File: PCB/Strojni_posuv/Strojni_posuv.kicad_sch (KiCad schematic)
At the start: 32 parts, among them SW1 SW_DPST_x2, SW2 SW_DPST_x2, SW3 SW_DPST_x2, SW4 SW_DPST_x2, SW5 SW_DPST_x2, U1 STM32F103RBTx

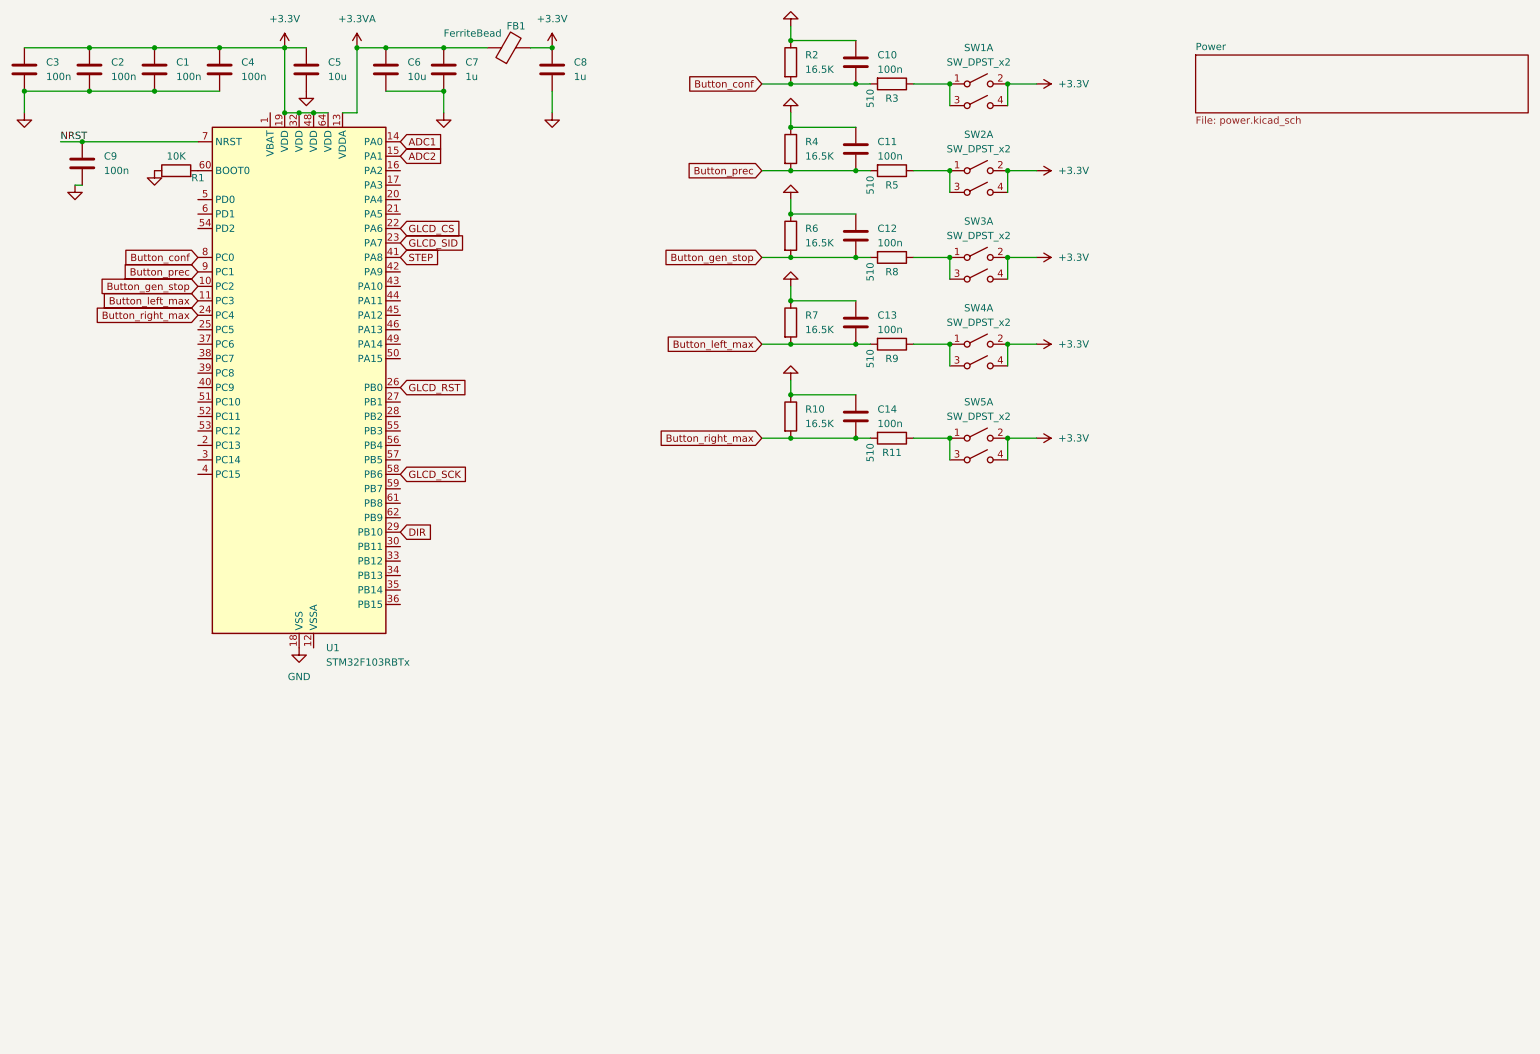
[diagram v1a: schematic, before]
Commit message: Learning, PCB making #2 Added new links to Learning Motor driver part in Kicad, Power part (48V to 5V), New pins to STM32F103
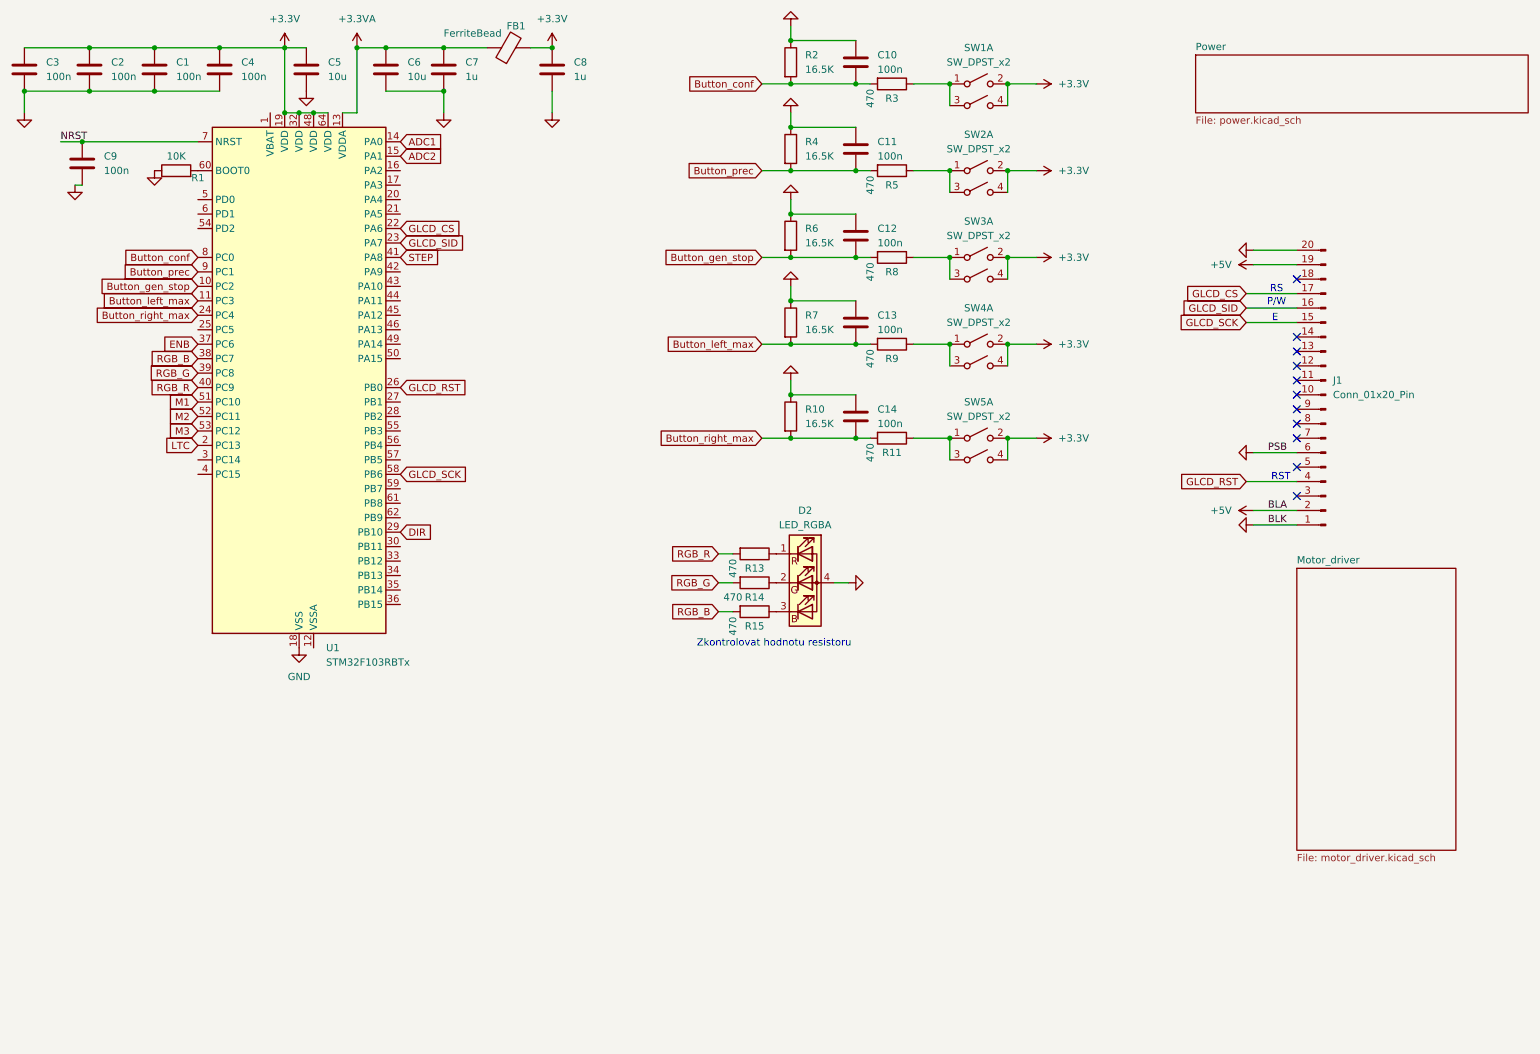
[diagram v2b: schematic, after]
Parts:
- added D2: LED_RGBA, symbol Device:LED_RGBA
- added J1: Conn_01x20_Pin, symbol Connector:Conn_01x20_Pin
- added R13, R14, R15: 470, symbol Device:R
- R11, R3, R5, R8, R9: value 510 -> 470
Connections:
- net GLCD_CS: now also J1.17 (Pin_17)
- net GLCD_RST: now also J1.4 (Pin_4)
- net GLCD_SCK: now also J1.15 (Pin_15)
- net GLCD_SID: now also J1.16 (Pin_16)
- net GND: now also D2.4 (A), J1.1 (Pin_1), J1.20 (Pin_20), J1.6 (Pin_6)
- net LTC: now reaches U1.2 (PC13)
- net ENB: now reaches U1.37 (PC6)
- net RGB_B: now reaches U1.38 (PC7)
- net RGB_B: now also R15.2
- net RGB_G: now reaches U1.39 (PC8)
- net RGB_G: now also R14.2
- net RGB_R: now reaches U1.40 (PC9)
- net RGB_R: now also R13.2
- net M1: now reaches U1.51 (PC10)
- net M2: now reaches U1.52 (PC11)
- net M3: now reaches U1.53 (PC12)
- new net: D2.2 (GK), R14.1
- new net: D2.1 (RK), R13.1
- new net: D2.3 (BK), R15.1
- new net +5V: J1.19 (Pin_19), J1.2 (Pin_2)
- no-connect marks 0 -> 11
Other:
- added sheet Motor_driver (motor_driver.kicad_sch)
- note added: "E"
- note added: "P/W"
- note added: "RS"
- note added: "RST"
- note added: "Zkontrolovat hodnotu resistoru"

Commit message: PCB making #3 Whole motor driver, small power changes, STM32 clock and new pin configuration
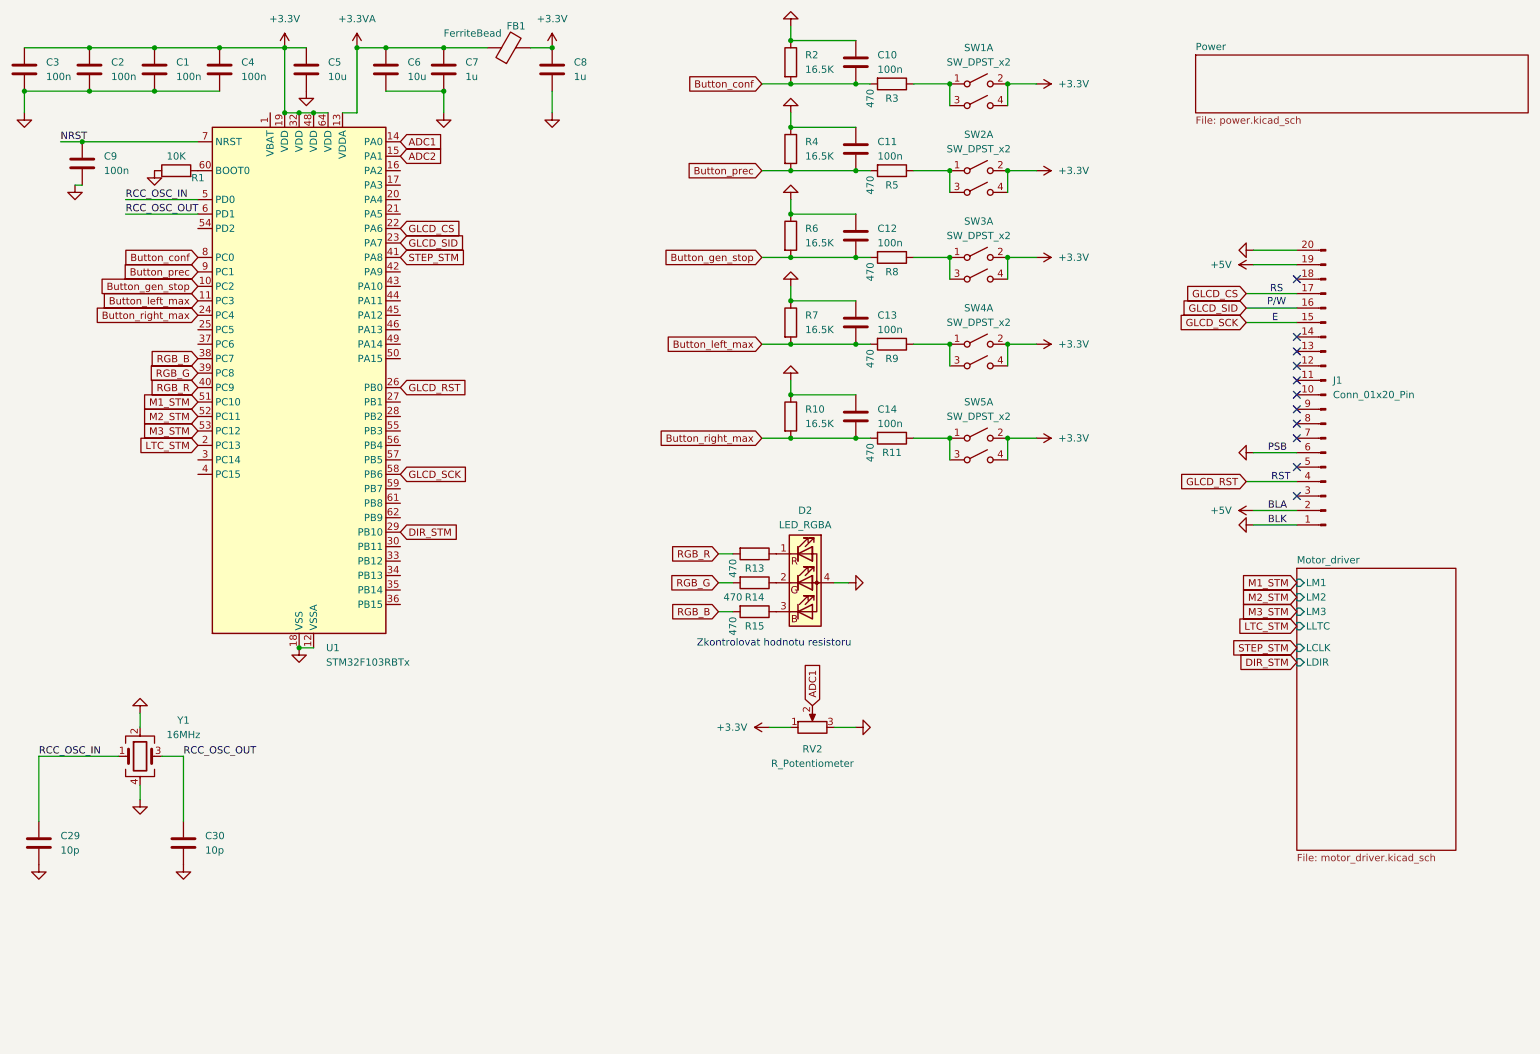
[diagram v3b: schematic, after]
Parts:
- added C29, C30: 10p, symbol Device:C
- added RV2: R_Potentiometer, symbol Device:R_Potentiometer
- added Y1: 16MHz, symbol Device:Crystal_GND24
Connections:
- net +3.3V: now also RV2.1
- net ADC1: now also RV2.2
- net GND: now also U1.12 (VSSA), C29.2, C30.2, RV2.3, Y1.2, Y1.4
- net RCC_OSC_IN: now reaches U1.5 (PD0)
- net RCC_OSC_IN: now also C29.1, Y1.1
- net RCC_OSC_OUT: now reaches U1.6 (PD1)
- net RCC_OSC_OUT: now also C30.1, Y1.3
- net DIR renamed DIR_STM
- net ENB: no longer names the net of U1.37 (PC6)
- net LTC renamed LTC_STM
- net M1 renamed M1_STM
- net M2 renamed M2_STM
- net M3 renamed M3_STM
- net STEP renamed STEP_STM
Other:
- sheet Motor_driver ports: added LCLK, LDIR, LLTC, LM1, LM2, LM3; removed none

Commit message: PCB making #4 Finding components on JLCPCB and adding their tags to schematic. Assigning almost all footprints
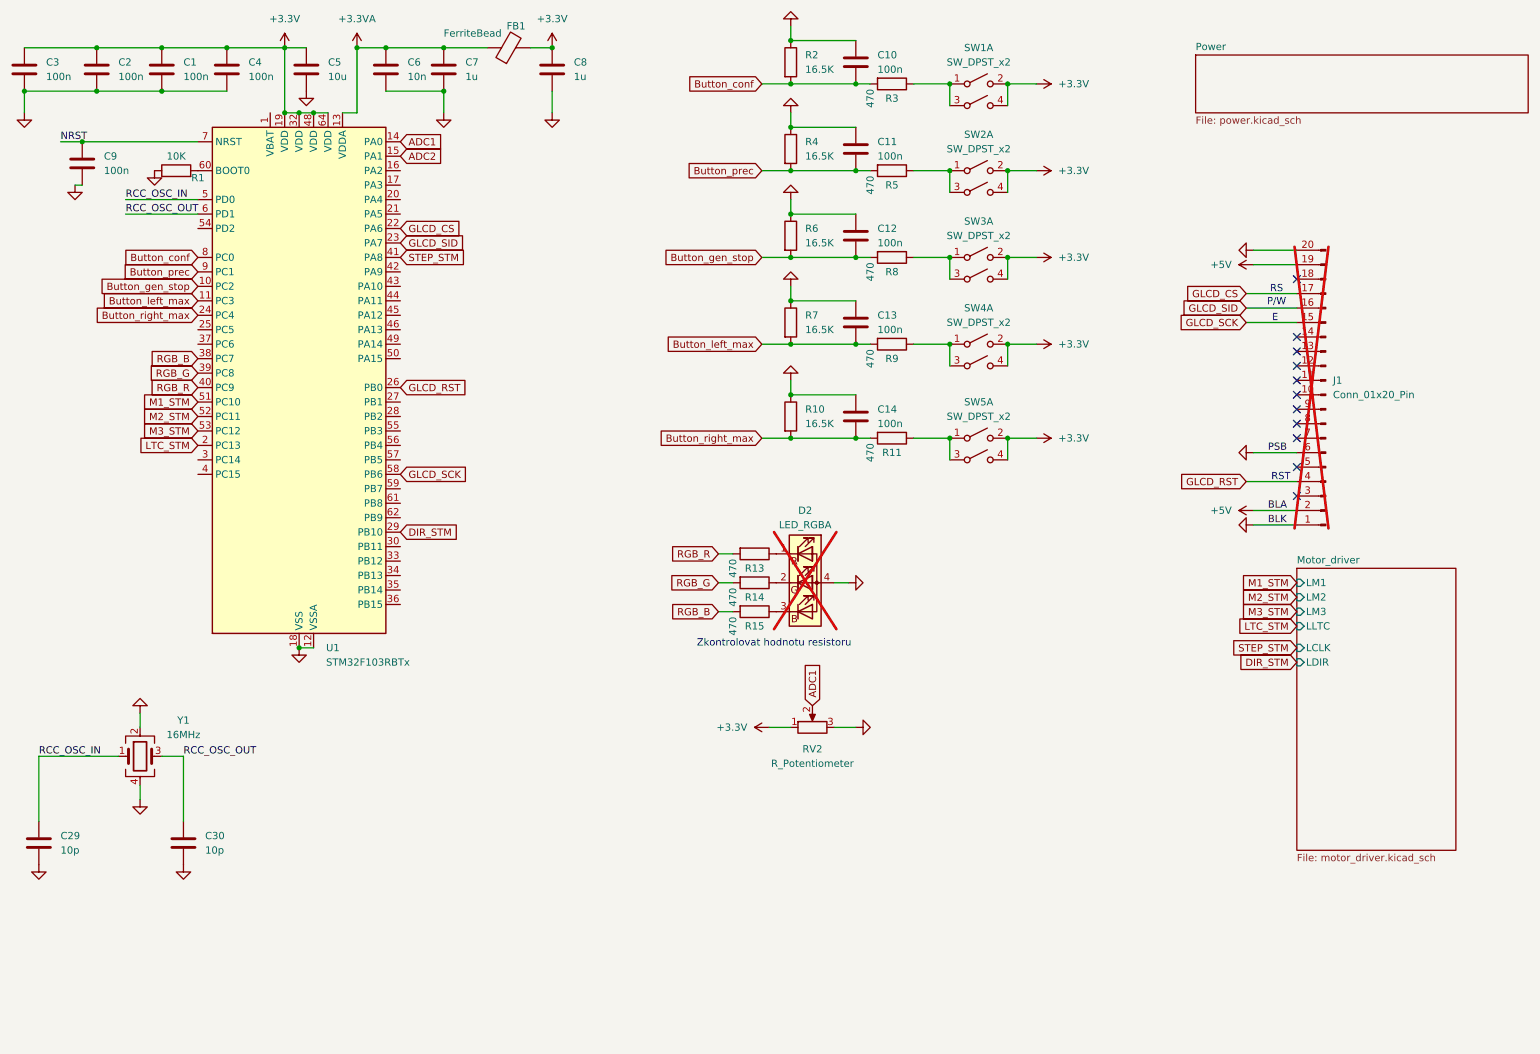
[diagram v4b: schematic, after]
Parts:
- C1, C10, C11, C12, C13, C14, C2, C3, C4, C9: footprint (none) -> Capacitor_SMD:C_0603_1608Metric; LCSC (none) -> C14663
- C29, C30: footprint (none) -> Capacitor_SMD:C_0603_1608Metric; LCSC (none) -> C1634
- C5: footprint (none) -> Capacitor_SMD:C_0805_2012Metric; LCSC (none) -> C307517
- C6: value 10u -> 10n; footprint (none) -> Capacitor_SMD:C_0603_1608Metric; LCSC (none) -> C100042
- C7, C8: footprint (none) -> Capacitor_SMD:C_0603_1608Metric; LCSC (none) -> C15849
- D2: footprint (none) -> LED_THT:LED_D5.0mm-4_RGB_Wide_Pins; now not fitted; now left out of the parts list
- FB1: footprint (none) -> Inductor_SMD:L_0603_1608Metric; LCSC (none) -> C1002
- J1: footprint (none) -> Connector_PinSocket_2.54mm:PinSocket_1x20_P2.54mm_Vertical; now not fitted; now left out of the parts list
- R1: footprint (none) -> Resistor_SMD:R_0603_1608Metric; LCSC (none) -> C25804
- R10, R2, R4, R6, R7: footprint (none) -> Resistor_SMD:R_0603_1608Metric; LCSC (none) -> C22812
- R11, R13, R14, R15, R3, R5, R8, R9: footprint (none) -> Resistor_SMD:R_0603_1608Metric; LCSC (none) -> C23179
- SW1, SW2, SW3, SW4, SW5: footprint (none) -> Button_Switch_THT:SW_PUSH_6mm
- Y1: footprint (none) -> Crystal:Crystal_SMD_3225-4Pin_3.2x2.5mm

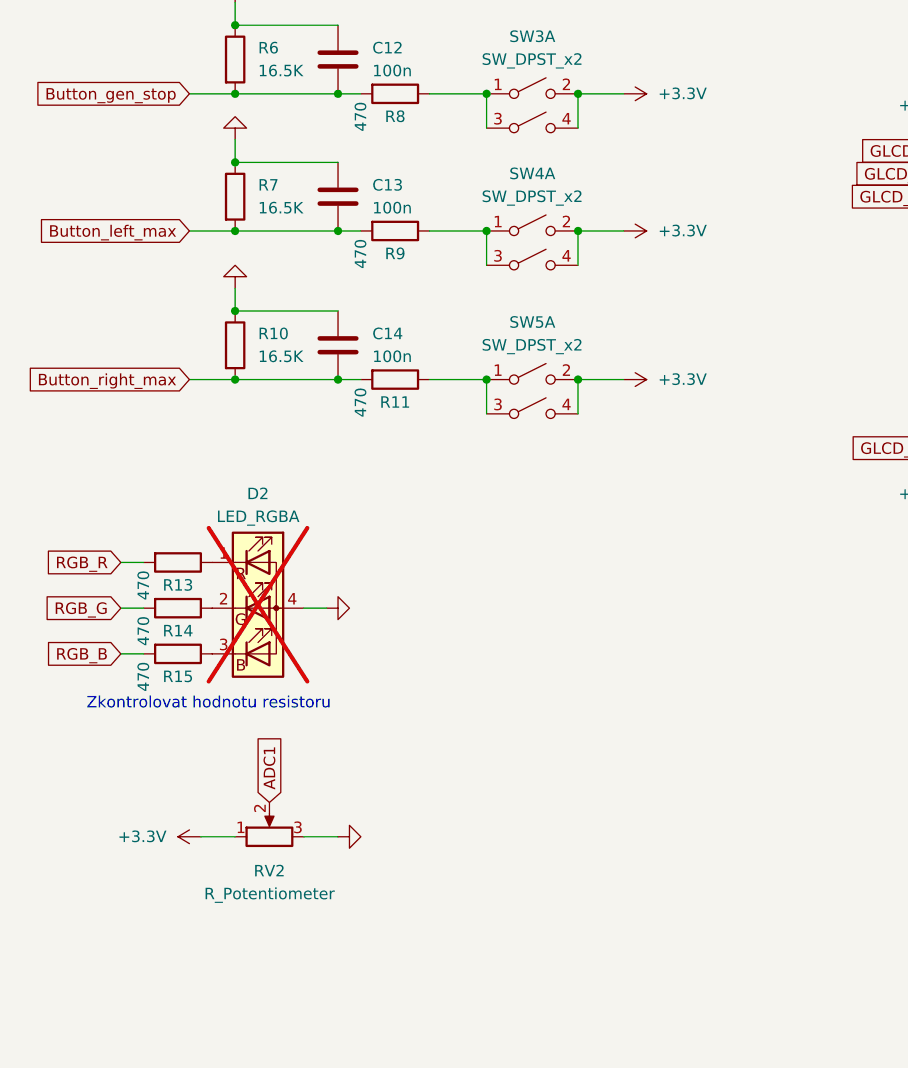
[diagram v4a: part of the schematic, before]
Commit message: PCB making #6 Placing all components - component layout
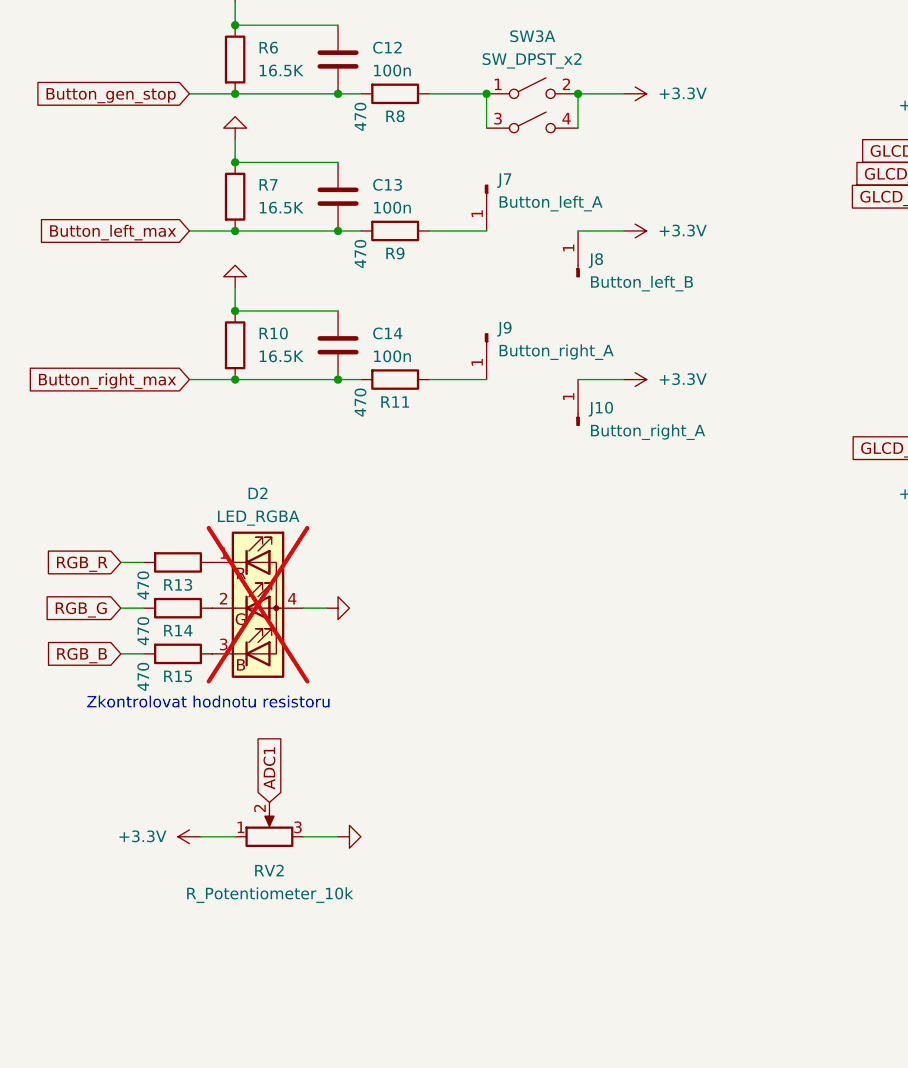
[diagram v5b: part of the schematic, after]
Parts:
- removed SW4, SW5: SW_DPST_x2, Button_Switch_THT:SW_PUSH_6mm, symbol Switch:SW_DPST_x2
- added J10, J9: Button_right_A, Connector_Pin:Pin_D1.3mm_L11.3mm_W2.8mm_Flat, symbol Connector:Conn_01x01_Pin
- added J7: Button_left_A, Connector_Pin:Pin_D1.3mm_L11.3mm_W2.8mm_Flat, symbol Connector:Conn_01x01_Pin
- added J8: Button_left_B, Connector_Pin:Pin_D1.3mm_L11.3mm_W2.8mm_Flat, symbol Connector:Conn_01x01_Pin
- RV2: value R_Potentiometer -> R_Potentiometer_10k; footprint (none) -> Potentiometer_THT:Potentiometer_Alps_RK09K_Single_Vertical; LCSC (none) -> C209779
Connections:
- net +3.3V: now also J10.1 (Pin_1), J8.1 (Pin_1)
- net at R11.1: now also J9.1 (Pin_1)
- net at R9.1: now also J7.1 (Pin_1)
